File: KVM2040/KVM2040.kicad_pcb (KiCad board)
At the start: 2 copper layers, 30 x 20 mm, 3 parts, among them J1 HDMI_A_1.4, U1 RP2040, U2 TS3DV642A0RUAR

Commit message: USB progress
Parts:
- added C1: 0.1uF, Capacitor_SMD:C_0603_1608Metric, F.Cu at (204.1, 76.2)
- added C2: 0.001uF, Capacitor_SMD:C_0603_1608Metric, F.Cu at (204.1, 78.7)
- added J2: USB4056-03-A, USB4056:USB4056-03-A, F.Cu at (228.6, 59.0)
- added J3: USB4056-03-A, USB4056:USB4056-03-A, F.Cu at (215.5, 59.0)
- added R1: 1M, Resistor_SMD:R_0402_1005Metric, F.Cu at (203.6, 81.0)
- added U3: XTMUXHS4212RKSR, TMUXHS4212:XTMUXHS4212RKSR, F.Cu at (219.1, 69.4)
- added U4: PTMUXHS221NKGR, TMUXHS221:PTMUXHS221NKGR, F.Cu at (209.4, 66.2)
- J1: value HDMI_A_1.4 -> SS-52000-003; footprint Connector_HDMI:HDMI_A_Molex_208658-1001_Horizontal -> SS-52000:SS-52000-003
- U1: value RP2040 -> TUSB8042AIRGCR; footprint Package_DFN_QFN:QFN-56-1EP_7x7mm_P0.4mm_EP3.2x3.2mm -> TUSB8042A:TUSB8042AIRGCR
- U2: value TS3DV642A0RUAR -> SIT8008BC-71-18S-24.000000; footprint TS3DV642:TS3DV642A0RUAR -> SIT8008BC:SIT8008BC-71-18S-24.000000
- moved U1 93.8 mm to (229.0, 83.8)
- moved J1 86.4 mm to (237.9, 66.3), turned to 180 degrees
- moved U2 74.5 mm to (225.7, 76.5), turned to 0 degrees
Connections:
- J1 pad 1: /D2+ -> GND
- J1 pad 10: /CK+ -> unconnected-(J1-Pad10)
- J1 pad 12: /CK- -> unconnected-(J1-Pad12)
- J1 pad 13: /CEC -> unconnected-(J1-Pad13)
- J1 pad 14: /UTILITY -> +5V
- J1 pad 15: /SCL -> unconnected-(J1-Pad15)
- J1 pad 16: /SDA -> unconnected-(J1-Pad16)
- J1 pad 18: +5V -> unconnected-(J1-Pad18)
- J1 pad 2: GND -> unconnected-(J1-Pad2)
- J1 pad 3: /D2- -> unconnected-(J1-Pad3)
- J1 pad 4: /D1+ -> +5V
- J1 pad 5: GND -> unconnected-(J1-Pad5)
- J1 pad 6: /D1- -> unconnected-(J1-Pad6)
- J1 pad 7: /D0+ -> GND
- J1 pad 8: GND -> unconnected-(J1-Pad8)
- U1 pad 1: Net-(U1-IOVDD-Pad1) -> unconnected-(U1-USB_DP_DN1-Pad1)
- U1 pad 10: Net-(U1-IOVDD-Pad1) -> unconnected-(U1-USB_DM_DN2-Pad10)
- U1 pad 2: /EN -> unconnected-(U1-USB_DM_DN1-Pad2)
- U1 pad 22: Net-(U1-IOVDD-Pad1) -> unconnected-(U1-USB_SSRXP_DN3-Pad22)
- U1 pad 23: Net-(U1-DVDD-Pad23) -> unconnected-(U1-USB_SSRXM_DN3-Pad23)
- U1 pad 3: /SEL1 -> unconnected-(U1-USB_SSTXP_DN1-Pad3)
- U1 pad 33: Net-(U1-IOVDD-Pad1) -> unconnected-(U1-PWRCTL3/BATEM/-Pad33)
- U1 pad 4: /SEL2 -> unconnected-(U1-USB_SSTXM_DN1-Pad4)
- U1 pad 42: Net-(U1-IOVDD-Pad1) -> unconnected-(U1-GANGED/SMBA2/HS_UP-Pad42)
- U1 pad 48: unconnected-(U1-USB_VDD-Pad48) -> VBUS
- U1 pad 49: Net-(U1-IOVDD-Pad1) -> unconnected-(U1-TEST-Pad49)
- U1 pad 50: Net-(U1-DVDD-Pad23) -> unconnected-(U1-GRSTz-Pad50)
- U2 pad 1: +5V -> unconnected-(U2-OE/ST/NC-Pad1)
- U2 pad 2: /EN -> GND
- U2 pad 3: /SCL -> /USB_Switch/XI
- U2 pad 4: /SDA -> +3.3V
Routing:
- net VBUS: track 0.00 -> 2.47 mm
- net GND: track 0.00 -> 2.47 mm
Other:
- board size 30 x 20 mm -> 100 x 50 mm

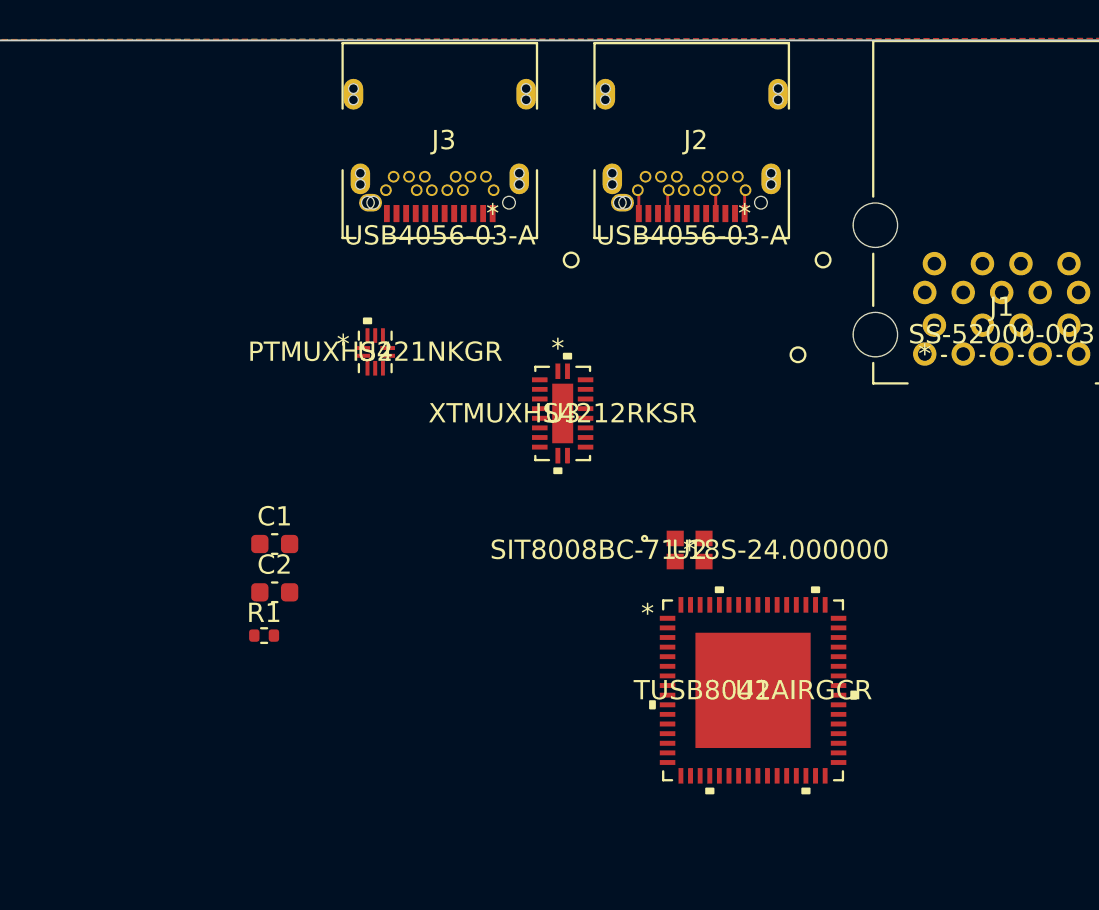
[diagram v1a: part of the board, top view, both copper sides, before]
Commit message: USB-B replacement
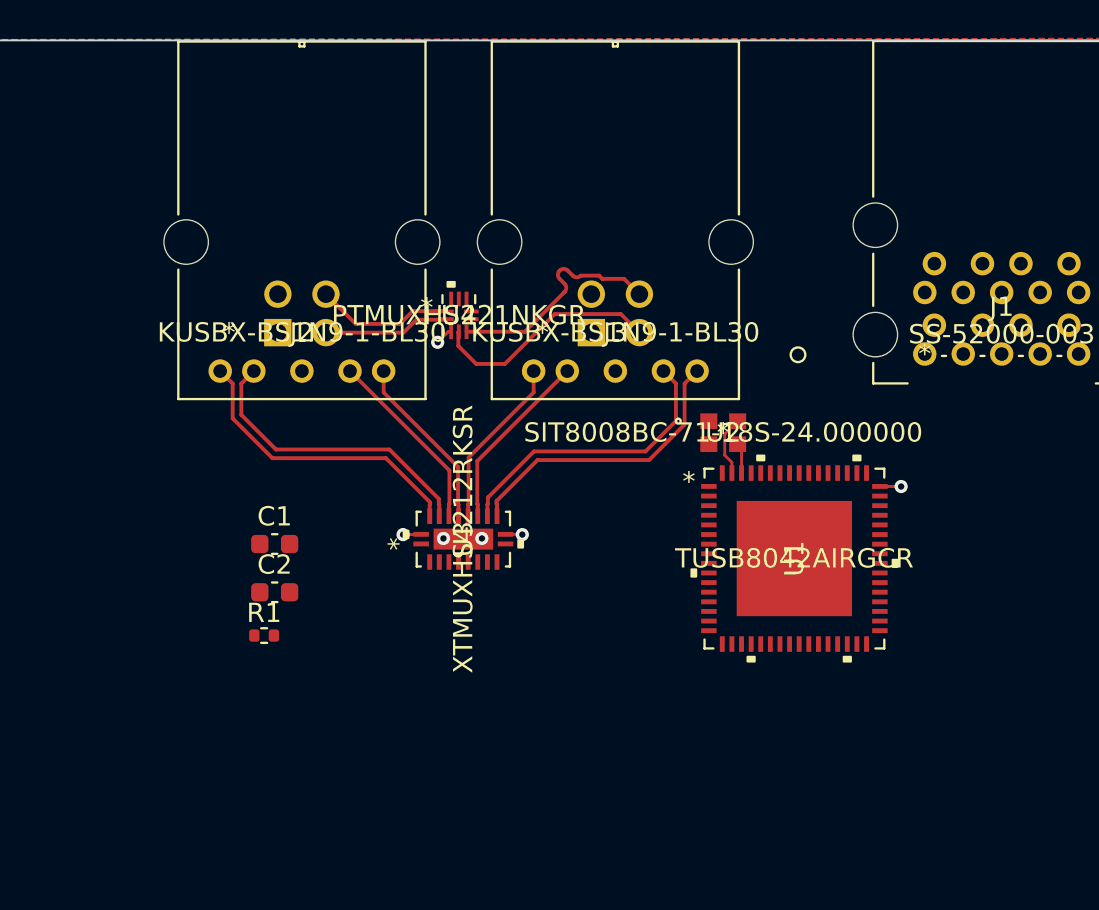
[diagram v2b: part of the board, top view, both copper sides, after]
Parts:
- J2, J3: value USB4056-03-A -> KUSBX-BS1N9-1-BL30; footprint USB4056:USB4056-03-A -> KUSBX-BS1N9:KUSBX-BS1N9-1-BL30
- moved J2 25.0 mm to (204.3, 65.2), turned to 0 degrees
- moved U3 8.33 mm to (213.9, 75.9), turned to 90 degrees
- moved J3 8.04 mm to (220.6, 65.2), turned to 0 degrees
- moved U1 7.18 mm to (231.2, 76.9)
- moved U2 6.35 mm to (227.4, 70.4)
- moved U4 4.74 mm to (213.7, 64.3)
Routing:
- net /USB_Switch/SSRX_A+: track 0.00 -> 15.5 mm
- net /USB_Switch/SSRX_A-: track 0.00 -> 15.5 mm
- net /USB_Switch/SSTX_B-: track 0.00 -> 15.3 mm
- net /USB_Switch/SSTX_B+: track 0.00 -> 15.3 mm
- net /USB_Switch/D_B-: track 0.00 -> 12.0 mm
- net /USB_Switch/D_B+: track 0.11 -> 12.0 mm
- net /USB_Switch/SSTX_A+: track 0.00 -> 9.70 mm
- net /USB_Switch/SSRX_B-: track 0.00 -> 9.50 mm
- net /USB_Switch/SSTX_A-: track 0.00 -> 9.16 mm
- net /USB_Switch/SSRX_B+: track 0.00 -> 8.96 mm
- net /USB_Switch/D_A+: track 0.00 -> 7.19 mm
- net /USB_Switch/D_A-: track 0.00 -> 6.55 mm
- net +3.3V: track 0.00 -> 3.13 mm
- net /USB_Switch/XI: track 0.00 -> 1.58 mm
- net VBUS: track 2.47 -> 1.11 mm, vias 0 -> 1
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- added copper zone on In1.Cu, net GND
- added copper zone on In2.Cu, net VBUS
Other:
- copper layers 2 -> 4
